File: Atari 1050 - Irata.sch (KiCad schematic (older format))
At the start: 13 parts, among them J2 Conn_01x05, U5 74LS00, U6 74LS00

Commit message: Initial commit
Added main logic
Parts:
- gave numbers to parts that had none: 3
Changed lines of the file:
@@
 	5350 4050 5350 3700
 $Comp
-L 74xx:74LS139 U?
+L 74xx:74LS139 U7
 U 1 1 6226CCAA
 P 3100 2350
-F 0 "U?" H 3100 2717 50  0000 C CNN
+F 0 "U7" H 3100 2717 50  0000 C CNN
 F 1 "74LS139" H 3100 2626 50  0000 C CNN
 F 2 "" H 3100 2350 50  0001 C CNN
@@
 $EndComp
 $Comp
-L 74xx:74LS139 U?
+L 74xx:74LS139 U7
 U 2 1 6226DDE8
 P 3100 1550
-F 0 "U?" H 3100 1917 50  0000 C CNN
+F 0 "U7" H 3100 1917 50  0000 C CNN
 F 1 "74LS139" H 3100 1826 50  0000 C CNN
 F 2 "" H 3100 1550 50  0001 C CNN
@@
 $EndComp
 $Comp
-L 74xx:74LS42 U?
+L 74xx:74LS42 U4
 U 1 1 6226EA68
 P 3050 3850
-F 0 "U?" H 2800 4400 50  0000 C CNN
+F 0 "U4" H 2800 4400 50  0000 C CNN
 F 1 "74LS42" H 3300 4400 50  0000 C CNN
 F 2 "" H 3050 3850 50  0001 C CNN
@@
 	5050 2450 3600 2450
 $Comp
-L 74xx:74LS30 U?
+L 74xx:74LS30 U8
 U 1 1 622B3855
 P 4750 4050
-F 0 "U?" H 4750 4575 50  0000 C CNN
+F 0 "U8" H 4750 4575 50  0000 C CNN
 F 1 "74LS30" H 4750 4484 50  0000 C CNN
 F 2 "" H 4750 4050 50  0001 C CNN

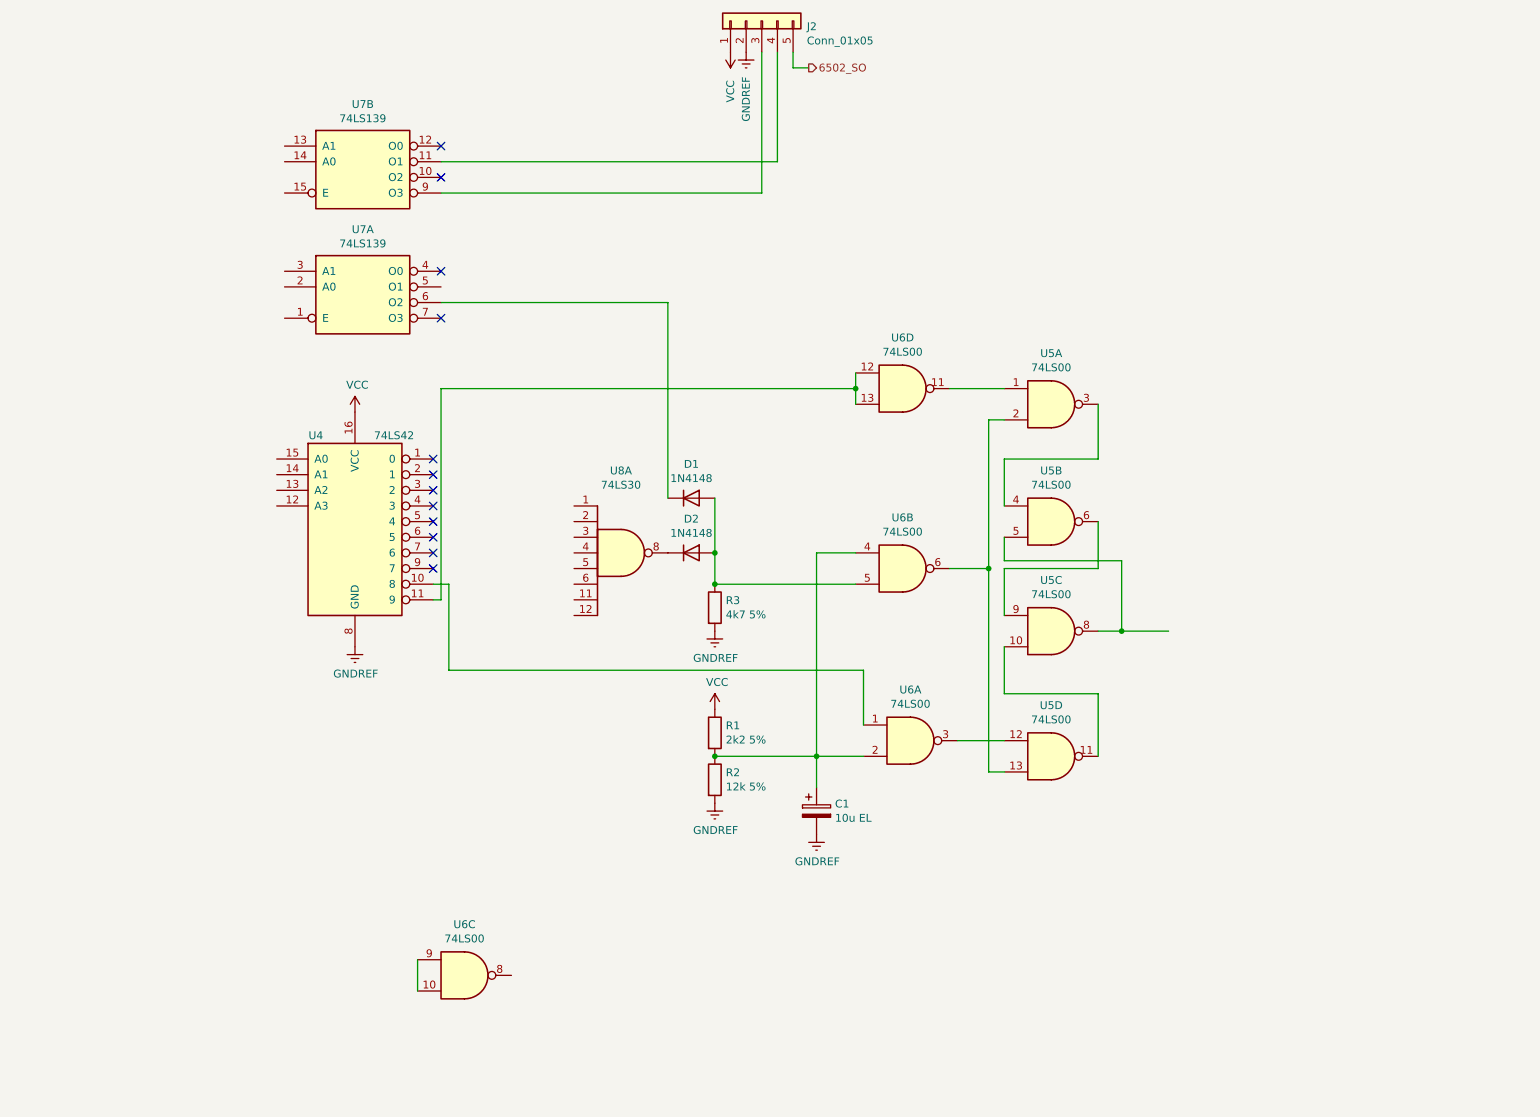
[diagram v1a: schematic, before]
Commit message: Corrections & Memories
* Corrected errors in the logic
* Added 2764 EPROM and 6264 SRAM (with connector symbol)
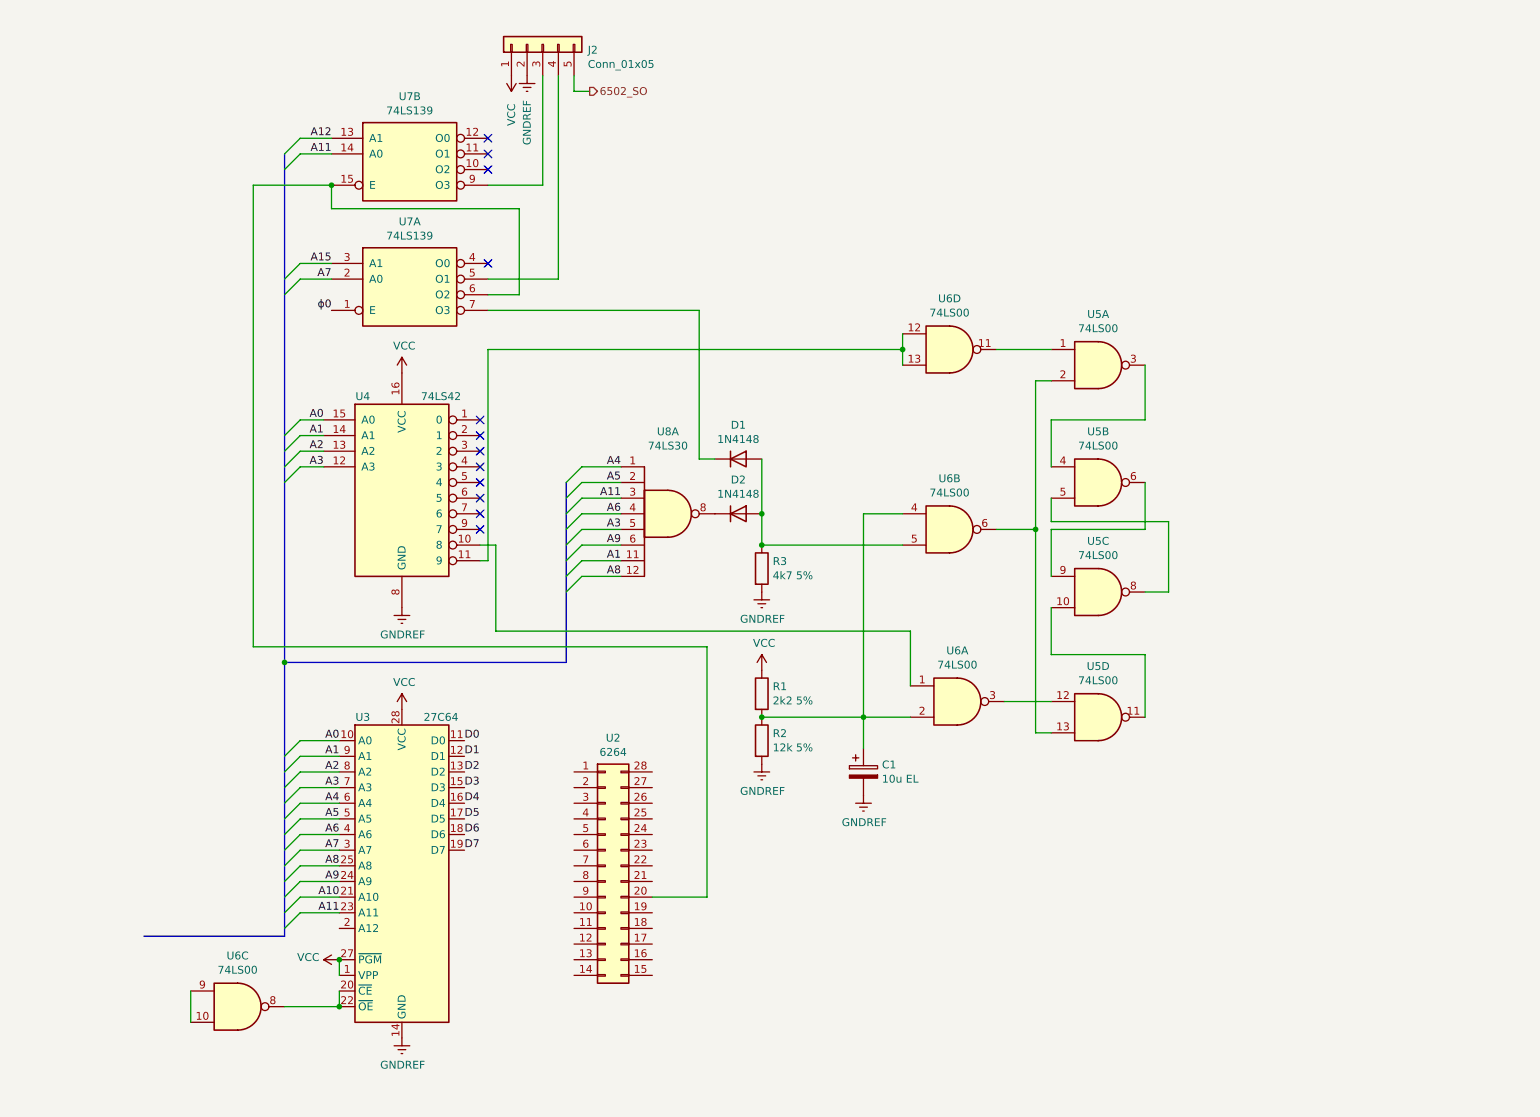
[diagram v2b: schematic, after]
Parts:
- added U2: 6264, symbol Connector_Generic:Conn_02x14_Counter_Clockwise
- added U3: 27C64, Package_DIP:DIP-28_W15.24mm, symbol Memory_EPROM:27C64
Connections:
- net GNDREF: now also U3.14 (GND)
- net VCC: now also U3.1 (VPP), U3.27 (~PGM), U3.28 (VCC)
- net at U6.8: now also U3.20 (~CE), U3.22 (~OE)
- net at D1.1 (K): now also U7.7 (O3); no longer U7.6 (O2)
- net ϕ0: now reaches U7.1 (E)
- net A7: now reaches U7.2 (A0)
- net A7: now also U3.3 (A7)
- net A15: now reaches U7.3 (A1)
- net at U7.5 (O1): now also J2.4 (Pin_4)
- net at U7.11 (O1): no longer J2.4 (Pin_4)
- net A12: now reaches U7.13 (A1)
- net A11: now reaches U7.14 (A0)
- net A11: now also U8.3, U3.23 (A11)
- net at U7.15 (E): now also U7.6 (O2), U2.20 (Pin_20)
- net A3: now reaches U4.12 (A3)
- net A3: now also U8.5, U3.7 (A3)
- net A2: now reaches U4.13 (A2)
- net A2: now also U3.8 (A2)
- net A1: now reaches U4.14 (A1)
- net A1: now also U8.11, U3.9 (A1)
- net A0: now reaches U4.15 (A0)
- net A0: now also U3.10 (A0)
- net A4: now reaches U8.1
- net A4: now also U3.6 (A4)
- net A8: now reaches U8.12
- net A8: now also U3.25 (A8)
- net A5: now reaches U8.2
- net A5: now also U3.5 (A5)
- net A6: now reaches U8.4
- net A6: now also U3.4 (A6)
- net A9: now reaches U8.6
- net A9: now also U3.24 (A9)
- new net A10: U3.21 (A10)
- new net D0: U3.11 (D0)
- new net D1: U3.12 (D1)
- new net D2: U3.13 (D2)
- new net D3: U3.15 (D3)
- new net D4: U3.16 (D4)
- new net D5: U3.17 (D5)
- new net D6: U3.18 (D6)
- new net D7: U3.19 (D7)
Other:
- moved on the sheet: C1, D1, D2, J2, R1, R2, R3, U4, U5A, U5B, U5C, U5D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

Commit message: CPU and main connector
* Added 6502 CPU (U1)
* Added 6507 pin-compatible connector (J1)
* Added data bus between existing circuit and added elements
*Added address bus between existing circuit and added elements
*Added control bus between U1 and J1
* Overall circuit displaced to the right in order to center drawing in the sheet
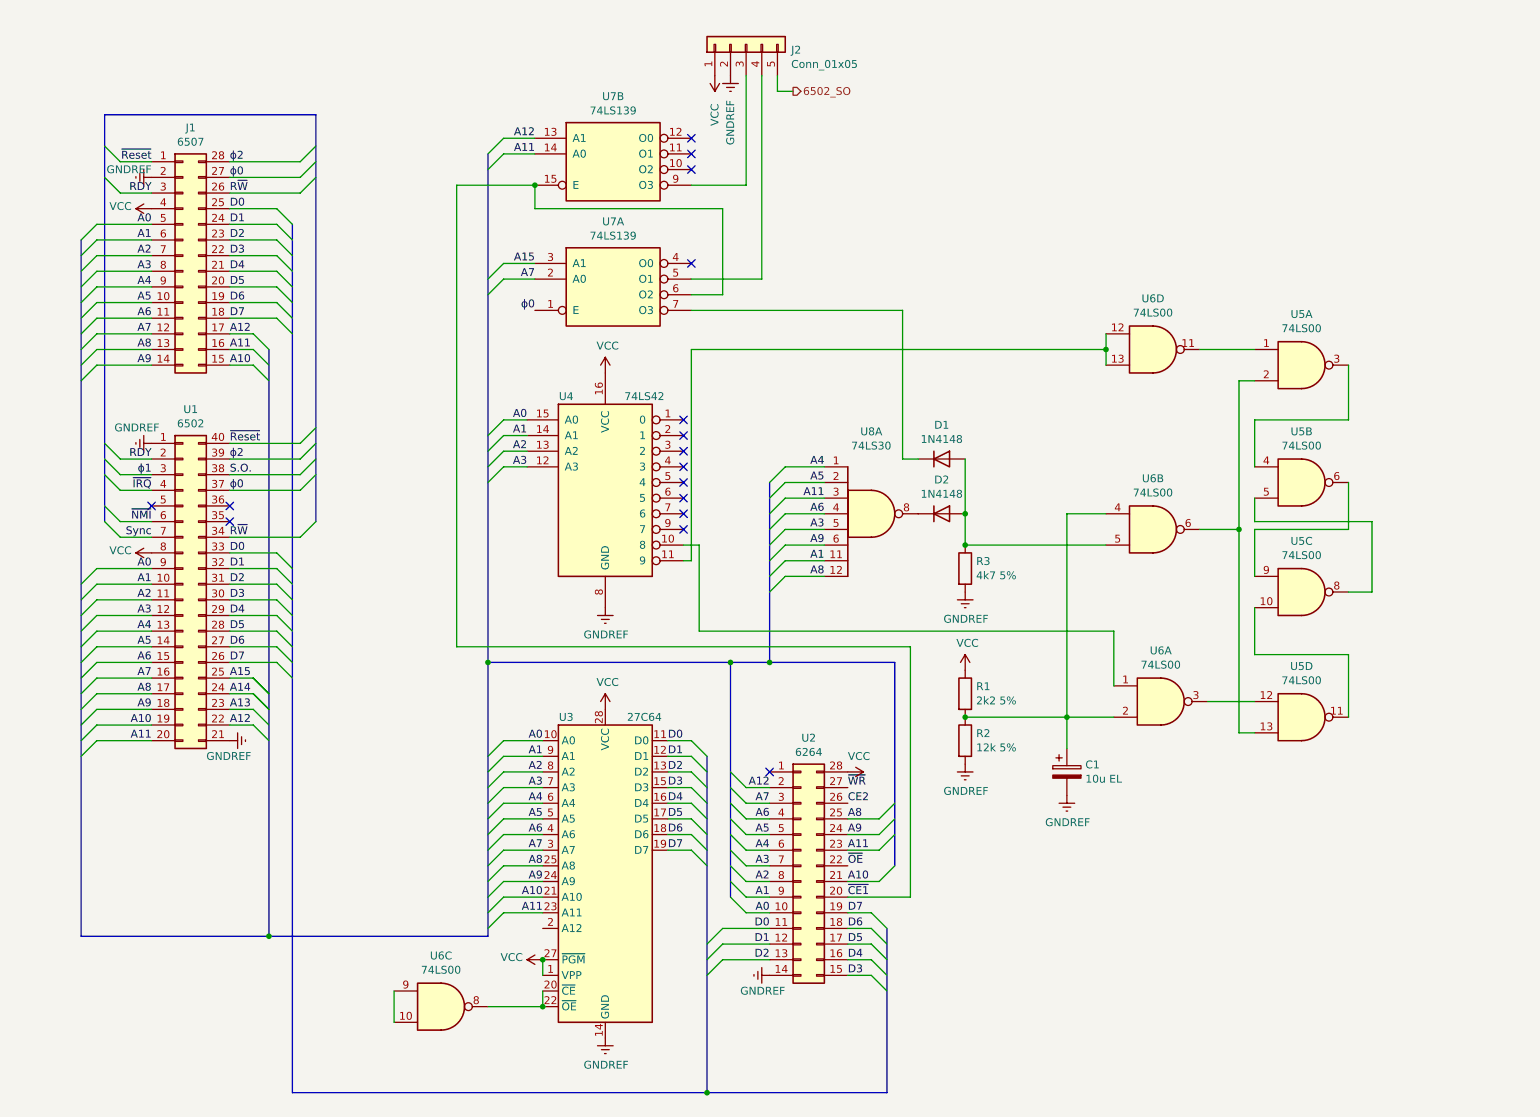
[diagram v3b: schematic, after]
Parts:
- added J1: 6507, symbol Connector_Generic:Conn_02x14_Counter_Clockwise
- added U1: 6502, symbol Connector_Generic:Conn_02x20_Counter_Clockwise
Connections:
- net A0: now also U2.10 (Pin_10), J1.5 (Pin_5), U1.9 (Pin_9)
- net A1: now also U2.9 (Pin_9), J1.6 (Pin_6), U1.10 (Pin_10)
- net A10: now also U2.21 (Pin_21), J1.15 (Pin_15), U1.19 (Pin_19)
- net A11: now also U2.23 (Pin_23), J1.16 (Pin_16), U1.20 (Pin_20)
- net A12: now also U2.2 (Pin_2), J1.17 (Pin_17), U1.22 (Pin_22)
- net A15: now also U1.25 (Pin_25)
- net A2: now also U2.8 (Pin_8), J1.7 (Pin_7), U1.11 (Pin_11)
- net A3: now also U2.7 (Pin_7), J1.8 (Pin_8), U1.12 (Pin_12)
- net A4: now also U2.6 (Pin_6), J1.9 (Pin_9), U1.13 (Pin_13)
- net A5: now also U2.5 (Pin_5), J1.10 (Pin_10), U1.14 (Pin_14)
- net A6: now also U2.4 (Pin_4), J1.11 (Pin_11), U1.15 (Pin_15)
- net A7: now also U2.3 (Pin_3), J1.12 (Pin_12), U1.16 (Pin_16)
- net A8: now also U2.25 (Pin_25), J1.13 (Pin_13), U1.17 (Pin_17)
- net A9: now also U2.24 (Pin_24), J1.14 (Pin_14), U1.18 (Pin_18)
- net D0: now also U2.11 (Pin_11), J1.25 (Pin_25), U1.33 (Pin_33)
- net D1: now also U2.12 (Pin_12), J1.24 (Pin_24), U1.32 (Pin_32)
- net D2: now also U2.13 (Pin_13), J1.23 (Pin_23), U1.31 (Pin_31)
- net D3: now also U2.15 (Pin_15), J1.22 (Pin_22), U1.30 (Pin_30)
- net D4: now also U2.16 (Pin_16), J1.21 (Pin_21), U1.29 (Pin_29)
- net D5: now also U2.17 (Pin_17), J1.20 (Pin_20), U1.28 (Pin_28)
- net D6: now also U2.18 (Pin_18), J1.19 (Pin_19), U1.27 (Pin_27)
- net D7: now also U2.19 (Pin_19), J1.18 (Pin_18), U1.26 (Pin_26)
- net GNDREF: now also U2.14 (Pin_14), J1.2 (Pin_2), U1.1 (Pin_1), U1.21 (Pin_21)
- net VCC: now also U2.28 (Pin_28), J1.4 (Pin_4), U1.8 (Pin_8)
- net ϕ0: now also J1.27 (Pin_27), U1.37 (Pin_37)
- net ~CE1: now reaches U2.20 (Pin_20), U7.15 (E), U7.6 (O2)
- net ~OE: now reaches U2.22 (Pin_22)
- net CE2: now reaches U2.26 (Pin_26)
- net ~WR: now reaches U2.27 (Pin_27)
- new net A13: U1.23 (Pin_23)
- new net A14: U1.24 (Pin_24)
- new net RDY: J1.3 (Pin_3), U1.2 (Pin_2)
- new net R~W: J1.26 (Pin_26), U1.34 (Pin_34)
- new net S.O.: U1.38 (Pin_38)
- new net Sync: U1.7 (Pin_7)
- new net ~IRQ: U1.4 (Pin_4)
- new net ~NMI: U1.6 (Pin_6)
- new net ~Reset: J1.1 (Pin_1), U1.40 (Pin_40)
- new net ϕ1: U1.3 (Pin_3)
- new net ϕ2: J1.28 (Pin_28), U1.39 (Pin_39)
- no-connect marks 12 -> 16
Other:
- moved on the sheet: C1, D1, D2, J2, R1, R2, R3, U2, U3, U4, U5A, U5B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

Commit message: Power
* Added power supplies for ICs U5-8
* Added decoupling capacitors C2, C3
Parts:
- added C2, C3: 2.2 TAN, symbol Device:CP
- added unit 5 of U5
- added unit 5 of U6
- added unit 3 of U7
- added unit 2 of U8
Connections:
- net GNDREF: now also C2.2, C3.2, U5.7 (GND), U6.7 (GND), U7.8 (GND), U8.7 (GND)
- net VCC: now also C2.1, C3.1, U5.14 (VCC), U6.14 (VCC), U7.16 (VCC), U8.14 (VCC)
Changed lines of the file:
@@
 Wire Wire Line
 	2250 3350 2700 3350
+$Comp
+L 74xx:74LS00 U5
+U 5 1 62C458DB
+P 7700 1350
+F 0 "U5" H 7930 1396 50  0000 L CNN
+F 1 "74LS00" H 7930 1305 50  0000 L CNN
+F 2 "" H 7700 1350 50  0001 C CNN
+F 3 "http://www.ti.com/lit/gpn/sn74ls00" H 7700 1350 50  0001 C CNN
+	5    7700 1350
+	1    0    0    -1
+$EndComp
+$Comp
+L 74xx:74LS00 U6
+U 5 1 62C4B322
+P 8450 1350
+F 0 "U6" H 8680 1396 50  0000 L CNN
+F 1 "74LS00" H 8680 1305 50  0000 L CNN
+F 2 "" H 8450 1350 50  0001 C CNN
+F 3 "http://www.ti.com/lit/gpn/sn74ls00" H 8450 1350 50  0001 C CNN
+	5    8450 1350
+	1    0    0    -1
+$EndComp
+$Comp
+L 74xx:74LS30 U8
+U 2 1 62C4DCF3
+P 10000 1350
+F 0 "U8" H 10230 1396 50  0000 L CNN
+F 1 "74LS30" H 10230 1305 50  0000 L CNN
+F 2 "" H 10000 1350 50  0001 C CNN
+F 3 "http://www.ti.com/lit/gpn/sn74LS30" H 10000 1350 50  0001 C CNN
+	2    10000 1350
+	1    0    0    -1
+$EndComp
+Wire Wire Line
+	7700 850  8450 850
+Wire Wire Line
+	9200 1850 8850 1850
+Connection ~ 8450 1850
+Wire Wire Line
+	8450 1850 7700 1850
+$Comp
+L power:VCC #PWR?
+U 1 1 62C86C90
+P 8850 850
+F 0 "#PWR?" H 8850 700 50  0001 C CNN
+F 1 "VCC" H 8865 1023 50  0000 C CNN
+F 2 "" H 8850 850 50  0001 C CNN
+F 3 "" H 8850 850 50  0001 C CNN
+	1    8850 850
+	1    0    0    -1
+$EndComp
+$Comp
+L power:GNDREF #PWR?
+U 1 1 62C88DBD
+P 8850 1850
+F 0 "#PWR?" H 8850 1600 50  0001 C CNN
+F 1 "GNDREF" H 8855 1677 50  0000 C CNN
+F 2 "" H 8850 1850 50  0001 C CNN
+F 3 "" H 8850 1850 50  0001 C CNN
+	1    8850 1850
+	1    0    0    -1
+$EndComp
+$Comp
+L 74xx:74LS139 U7
+U 3 1 62C9C3F8
+P 9200 1350
+F 0 "U7" H 9430 1396 50  0000 L CNN
+F 1 "74LS139" H 9430 1305 50  0000 L CNN
+F 2 "" H 9200 1350 50  0001 C CNN
+F 3 "http://www.ti.com/lit/ds/symlink/sn74ls139a.pdf" H 9200 1350 50  0001 C CNN
+	3    9200 1350
+	1    0    0    -1
+$EndComp
+Wire Wire Line
+	9200 1850 10000 1850
+Connection ~ 9200 1850
+Wire Wire Line
+	10000 850  9200 850
+Connection ~ 9200 850
+Connection ~ 8850 1850
+Wire Wire Line
+	8850 1850 8450 1850
+Wire Wire Line
+	8850 850  9200 850
+Wire Wire Line
+	8450 850  8850 850
+Connection ~ 8450 850
+Connection ~ 8850 850
+$Comp
+L Device:CP C2
+U 1 1 62D40000
+P 950 7200
+F 0 "C2" H 1068 7246 50  0000 L CNN
+F 1 "2.2 TAN" H 1068 7155 50  0000 L CNN
+F 2 "" H 988 7050 50  0001 C CNN
+F 3 "~" H 950 7200 50  0001 C CNN
+	1    950  7200
+	1    0    0    -1
+$EndComp
+$Comp
+L Device:CP C3
+U 1 1 62D4DB8B
+P 1550 7200
+F 0 "C3" H 1668 7246 50  0000 L CNN
+F 1 "2.2 TAN" H 1668 7155 50  0000 L CNN
+F 2 "" H 1588 7050 50  0001 C CNN
+F 3 "~" H 1550 7200 50  0001 C CNN
+	1    1550 7200
+	1    0    0    -1
+$EndComp
+Wire Wire Line
+	1550 7050 1250 7050
+$Comp
+L power:GNDREF #PWR?
+U 1 1 62D8654F
+P 1250 7350
+F 0 "#PWR?" H 1250 7100 50  0001 C CNN
+F 1 "GNDREF" H 1255 7177 50  0000 C CNN
+F 2 "" H 1250 7350 50  0001 C CNN
+F 3 "" H 1250 7350 50  0001 C CNN
+	1    1250 7350
+	1    0    0    -1
+$EndComp
+$Comp
+L power:VCC #PWR?
+U 1 1 62D8850E
+P 1250 7050
+F 0 "#PWR?" H 1250 6900 50  0001 C CNN
+F 1 "VCC" H 1265 7223 50  0000 C CNN
+F 2 "" H 1250 7050 50  0001 C CNN
+F 3 "" H 1250 7050 50  0001 C CNN
+	1    1250 7050
+	1    0    0    -1
+$EndComp
+Connection ~ 1250 7050
+Wire Wire Line
+	950  7050 1250 7050
+Connection ~ 1250 7350
+Wire Wire Line
+	1250 7350 1550 7350
+Wire Wire Line
+	950  7350 1250 7350
 Wire Bus Line
 	6500 4750 6500 6050
